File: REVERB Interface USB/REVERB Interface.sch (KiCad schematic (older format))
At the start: 72 parts, among them J1 RPiZeroW, J10 USBPWR, J2 Iridium, J3 APRS, J4 Antenna, J6 USB_B_Micro, J7 USB, J8 USBPOGO, J9 USB SWITCH, M1 Stack Mounting Hole, M2 Stack Mounting Hole, M3 Stack Mounting Hole, M4 Stack Mounting Hole, M5 PiMount, M6 PiMount, M7 PiMount, M8 PiMount, U1 IMU, U2 MAX3232, U3 CY7C65213-28PVXI, U4 TXB0104D, U5 DS3232M

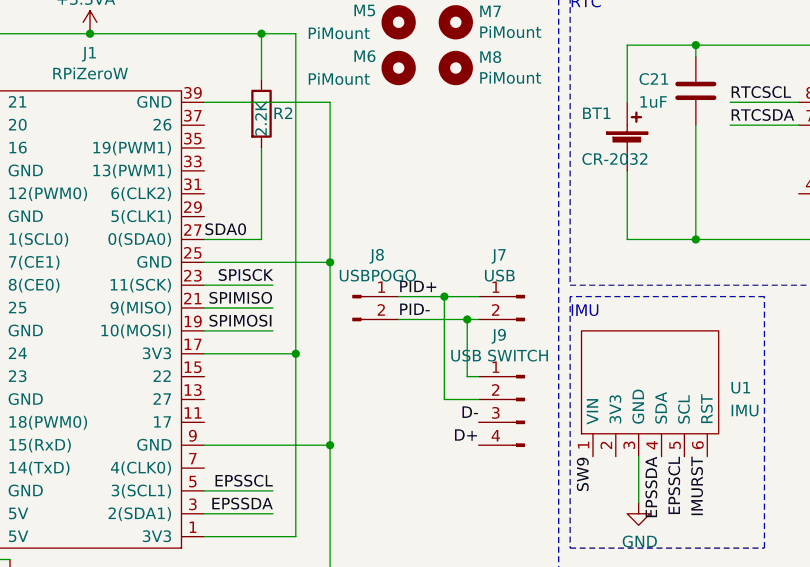
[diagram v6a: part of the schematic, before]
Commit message: remove usb pogo
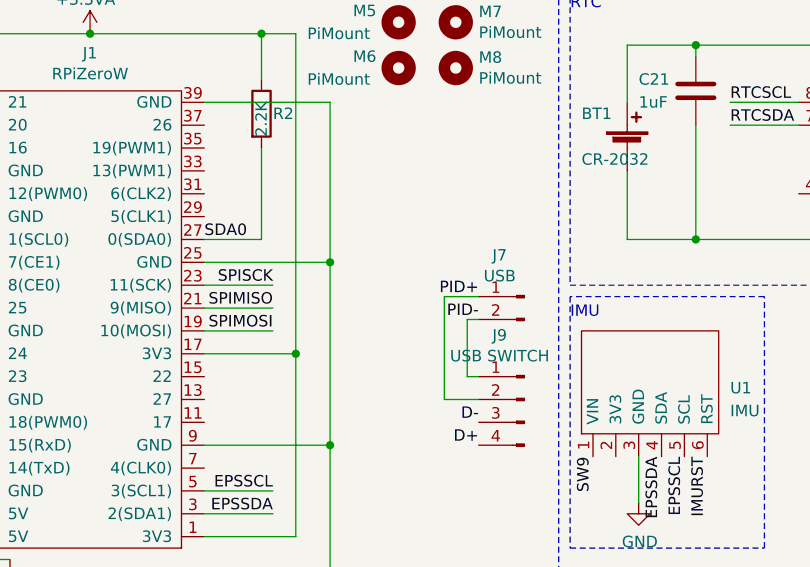
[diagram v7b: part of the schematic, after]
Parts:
- removed J8: USBPOGO, Connector_PinSocket_2.54mm:PinSocket_1x02_P2.54mm_Vertical, symbol Connector:Conn_01x02_Male
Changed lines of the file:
@@
 Text Notes 6700 5600 0    50   ~ 0
 Option 1: Hardware APRS, two converters to Iridium: \nJP1 and JP2 bridge pins 2 and 3, JP3 and JP4 bridge pins 1 and 2\nOption 2: USB UART APRS, MAX3232 Iridium:\nJP1 and JP2 bridge pins 1 and 2, JP3 and JP4 bridge pins 2 and 3\nDO NOT BRIDGE THE SAME TWO PINS FOR BOTH PAIRS OF JUMPERS
-$Comp
-L Connector:Conn_01x02_Male J8
-U 1 1 61634D7E
-P 6200 1850
-F 0 "J8" H 6308 2031 50  0000 C CNN
-F 1 "USBPOGO" H 6308 1940 50  0000 C CNN
-F 2 "Connector_PinSocket_2.54mm:PinSocket_1x02_P2.54mm_Vertical" H 6200 1850 50  0001 C CNN
-F 3 "~" H 6200 1850 50  0001 C CNN
-	1    6200 1850
-	1    0    0    -1
-$EndComp
-Text Label 6400 1850 0    50   ~ 0
+Text Label 6750 1850 2    50   ~ 0
 PID+
-Text Label 6400 1950 0    50   ~ 0
-PID-
 $Comp
 L Mechanical:MountingHole M5
@@
 	2850 2400 2250 2400
 Wire Wire Line
-	6400 1850 6600 1850
-Wire Wire Line
-	6400 1950 6700 1950
-Wire Wire Line
 	6750 2200 6700 2200
 Wire Wire Line
 	6700 2200 6700 1950
-Connection ~ 6700 1950
 Wire Wire Line
 	6700 1950 6750 1950
 Wire Wire Line
-	6600 1850 6600 2300
-Wire Wire Line
 	6600 2300 6750 2300
-Connection ~ 6600 1850
 Wire Wire Line
 	6600 1850 6750 1850
@@
 Wire Wire Line
 	9650 2850 9950 2850
+Wire Wire Line
+	6600 1850 6600 2300
+Text Label 6750 1950 2    50   ~ 0
+PID-
 $EndSCHEMATC
